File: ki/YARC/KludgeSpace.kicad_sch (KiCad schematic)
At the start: 7 parts

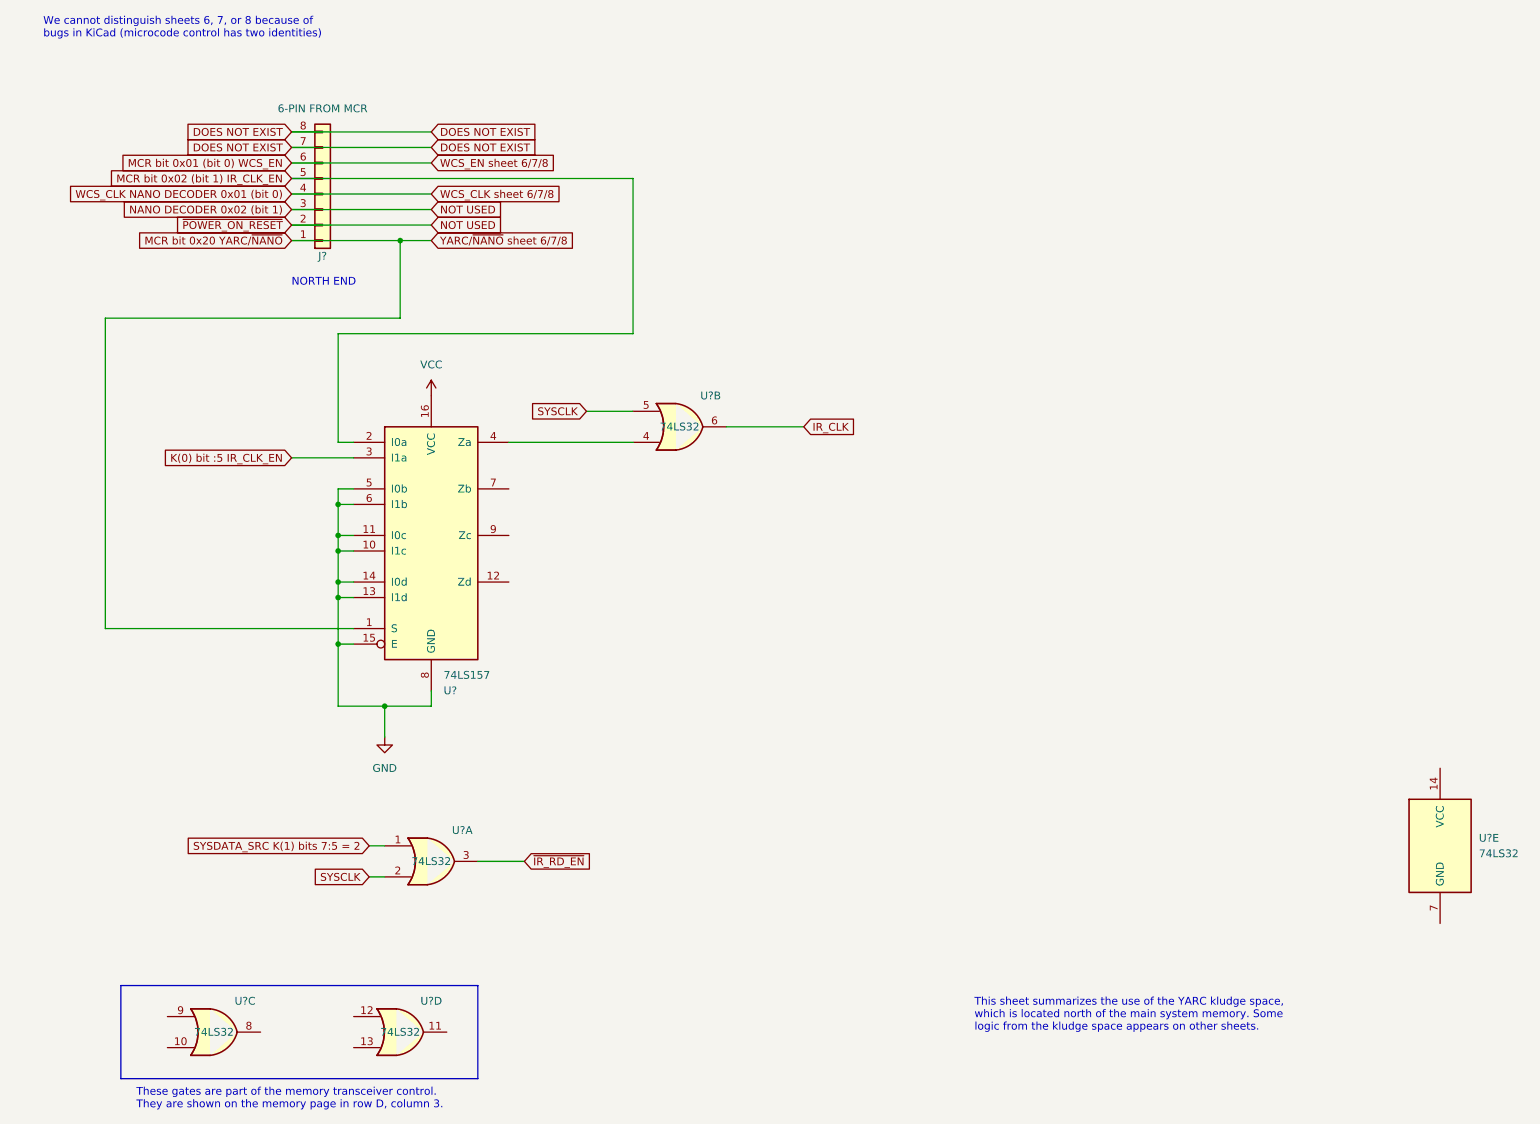
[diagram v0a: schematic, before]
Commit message: Assign part labels (U-numbers) in KiCad and start adding them to Fritzing layouts
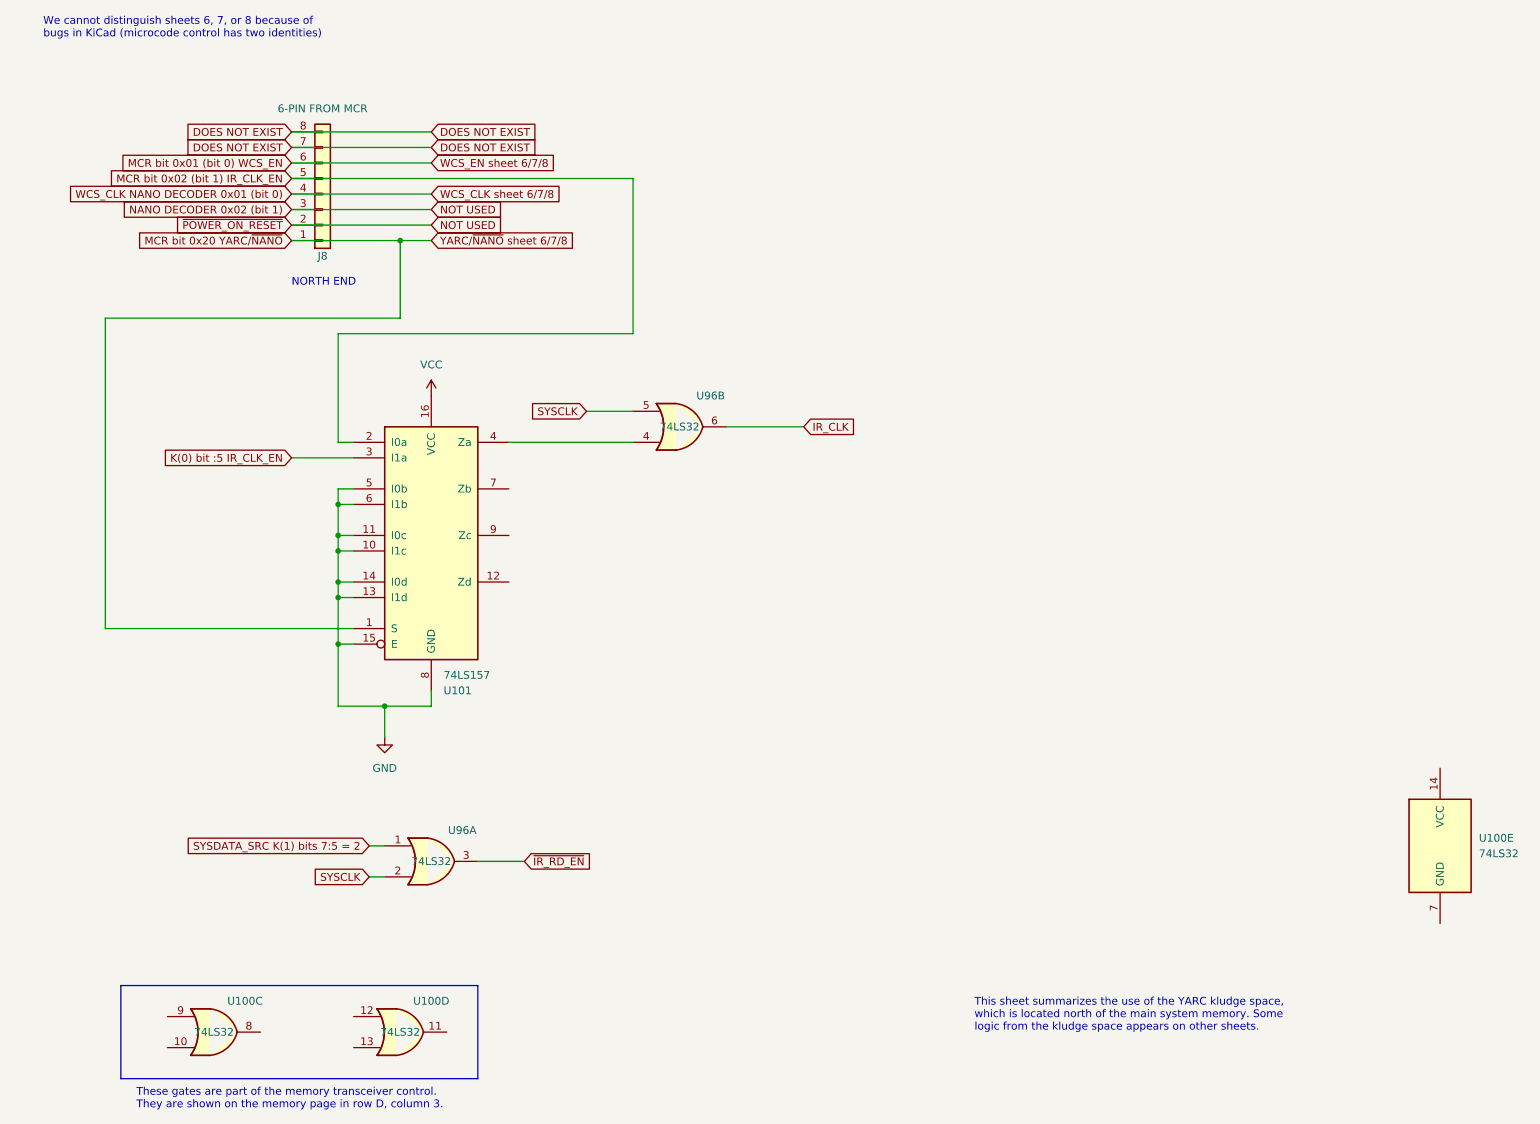
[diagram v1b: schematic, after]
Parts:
- gave numbers to parts that had none: 4
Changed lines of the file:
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@@
   (symbol (lib_id "74xx:74LS32") (at 73.66 182.88 0) (unit 4)
     (in_bom yes) (on_board yes)
-    (property "Reference" "U?" (id 0) (at 78.74 177.8 0))
+    (property "Reference" "U100" (id 0) (at 78.74 177.8 0))
     (property "Value" "74LS32" (id 1) (at 73.66 182.88 0))
     (property "Footprint" "" (id 2) (at 73.66 182.88 0)
@@
   (symbol (lib_id "power:VCC") (at 78.74 78.74 0) (unit 1)
     (in_bom yes) (on_board yes) (fields_autoplaced)
-    (property "Reference" "#PWR?" (id 0) (at 78.74 82.55 0)
+    (property "Reference" "#PWR0172" (id 0) (at 78.74 82.55 0)
       (effects (font (size 1.27 1.27)) hide)
     )
@@
   (symbol (lib_id "74xx:74LS32") (at 43.18 182.88 0) (unit 3)
     (in_bom yes) (on_board yes)
-    (property "Reference" "U?" (id 0) (at 48.26 177.8 0))
+    (property "Reference" "U100" (id 0) (at 48.26 177.8 0))
     (property "Value" "74LS32" (id 1) (at 43.18 182.88 0))
     (property "Footprint" "" (id 2) (at 43.18 182.88 0)
@@
   (symbol (lib_id "74xx:74LS32") (at 78.74 154.94 0) (unit 1)
     (in_bom yes) (on_board yes)
-    (property "Reference" "U?" (id 0) (at 83.82 149.86 0))
+    (property "Reference" "U96" (id 0) (at 83.82 149.86 0))
     (property "Value" "74LS32" (id 1) (at 78.74 154.94 0))
     (property "Footprint" "" (id 2) (at 78.74 154.94 0)
@@
   (symbol (lib_id "74xx:74LS32") (at 243.84 152.4 0) (unit 5)
     (in_bom yes) (on_board yes) (fields_autoplaced)
-    (property "Reference" "U?" (id 0) (at 250.19 151.1299 0)
+    (property "Reference" "U100" (id 0) (at 250.19 151.1299 0)
       (effects (font (size 1.27 1.27)) (justify left))
     )
@@
   (symbol (lib_id "74xx:74LS157") (at 78.74 101.6 0) (unit 1)
     (in_bom yes) (on_board yes) (fields_autoplaced)
-    (property "Reference" "U?" (id 0) (at 80.7594 127 0)
+    (property "Reference" "U101" (id 0) (at 80.7594 127 0)
       (effects (font (size 1.27 1.27)) (justify left))
     )
@@
   (symbol (lib_id "74xx:74LS32") (at 119.38 83.82 0) (mirror x) (unit 2)
     (in_bom yes) (on_board yes)
-    (property "Reference" "U?" (id 0) (at 124.46 78.74 0))
+    (property "Reference" "U96" (id 0) (at 124.46 78.74 0))
     (property "Value" "74LS32" (id 1) (at 119.38 83.82 0))
     (property "Footprint" "" (id 2) (at 119.38 83.82 0)
@@
   (symbol (lib_id "power:GND") (at 71.12 134.62 0) (unit 1)
     (in_bom yes) (on_board yes) (fields_autoplaced)
-    (property "Reference" "#PWR?" (id 0) (at 71.12 140.97 0)
+    (property "Reference" "#PWR0171" (id 0) (at 71.12 140.97 0)
       (effects (font (size 1.27 1.27)) hide)
     )
@@
   (symbol (lib_id "Connector_Generic:Conn_01x08") (at 60.96 45.72 0) (mirror x) (unit 1)
     (in_bom yes) (on_board yes)
-    (property "Reference" "J?" (id 0) (at 60.96 55.88 0))
+    (property "Reference" "J8" (id 0) (at 60.96 55.88 0))
     (property "Value" "6-PIN FROM MCR" (id 1) (at 60.96 31.75 0))
     (property "Footprint" "" (id 2) (at 60.96 45.72 0)

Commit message: Minor changes while wiring Port1 address transceiver
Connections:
- net GND: no longer U101.14 (I0d)
- net VCC: now also U101.14 (I0d)
- net ~{ADDRESS_XCVR_EN}: now reaches U101.12 (Zd)
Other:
- note added: "The effect of the "D" unit is merely to invert YARC/NANO# But it allows for future expansion (in case something else ever needs to drive the address bus when YARC)."
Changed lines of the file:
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@@
   (junction (at 63.5 119.38) (diameter 0) (color 0 0 0 0)
   )
+  (junction (at 78.74 78.74) (diameter 0) (color 0 0 0 0)
+  )
   (junction (at 63.5 101.6) (diameter 0) (color 0 0 0 0)
   )
@@
   (junction (at 63.5 104.14) (diameter 0) (color 0 0 0 0)
   )
+  (junction (at 63.5 111.76) (diameter 0) (color 0 0 0 0)
+  )
   (junction (at 73.66 53.34) (diameter 0) (color 0 0 0 0)
   )
-  (junction (at 63.5 111.76) (diameter 0) (color 0 0 0 0)
-  )
   (junction (at 71.12 129.54) (diameter 0) (color 0 0 0 0)
   )
-  (junction (at 63.5 109.22) (diameter 0) (color 0 0 0 0)
-  )
   (wire (pts (xy 104.14 81.28) (xy 111.76 81.28))
     (stroke (width 0) (type default) (color 0 0 0 0))
@@
     (stroke (width 0) (type default) (color 0 0 0 0))
   )
-  (wire (pts (xy 63.5 109.22) (xy 63.5 111.76))
-    (stroke (width 0) (type default) (color 0 0 0 0))
-  )
   (wire (pts (xy 66.04 101.6) (xy 63.5 101.6))
     (stroke (width 0) (type default) (color 0 0 0 0))
@@
     (stroke (width 0) (type default) (color 0 0 0 0))
   )
-  (wire (pts (xy 66.04 86.36) (xy 63.5 86.36))
+  (wire (pts (xy 58.42 86.36) (xy 66.04 86.36))
     (stroke (width 0) (type default) (color 0 0 0 0))
   )
@@
     (stroke (width 0) (type default) (color 0 0 0 0))
   )
-  (wire (pts (xy 63.5 119.38) (xy 63.5 111.76))
-    (stroke (width 0) (type default) (color 0 0 0 0))
-  )
   (wire (pts (xy 111.76 68.58) (xy 111.76 43.18))
     (stroke (width 0) (type default) (color 0 0 0 0))
   )
+  (wire (pts (xy 91.44 109.22) (xy 129.54 109.22))
+    (stroke (width 0) (type default) (color 0 0 0 0))
+  )
   (wire (pts (xy 73.66 53.34) (xy 78.74 53.34))
     (stroke (width 0) (type default) (color 0 0 0 0))
@@
     (stroke (width 0) (type default) (color 0 0 0 0))
   )
-  (wire (pts (xy 63.5 86.36) (xy 63.5 68.58))
-    (stroke (width 0) (type default) (color 0 0 0 0))
-  )
   (wire (pts (xy 55.88 53.34) (xy 73.66 53.34))
     (stroke (width 0) (type default) (color 0 0 0 0))
   )
+  (wire (pts (xy 60.96 109.22) (xy 60.96 78.74))
+    (stroke (width 0) (type default) (color 0 0 0 0))
+  )
   (wire (pts (xy 63.5 96.52) (xy 63.5 101.6))
     (stroke (width 0) (type default) (color 0 0 0 0))
@@
     (stroke (width 0) (type default) (color 0 0 0 0))
   )
+  (wire (pts (xy 91.44 86.36) (xy 111.76 86.36))
+    (stroke (width 0) (type default) (color 0 0 0 0))
+  )
+  (wire (pts (xy 58.42 68.58) (xy 58.42 86.36))
+    (stroke (width 0) (type default) (color 0 0 0 0))
+  )
+  (wire (pts (xy 78.74 48.26) (xy 55.88 48.26))
+    (stroke (width 0) (type default) (color 0 0 0 0))
+  )
   (wire (pts (xy 66.04 111.76) (xy 63.5 111.76))
     (stroke (width 0) (type default) (color 0 0 0 0))
   )
-  (wire (pts (xy 91.44 86.36) (xy 111.76 86.36))
-    (stroke (width 0) (type default) (color 0 0 0 0))
-  )
-  (wire (pts (xy 78.74 48.26) (xy 55.88 48.26))
-    (stroke (width 0) (type default) (color 0 0 0 0))
-  )
   (wire (pts (xy 78.74 50.8) (xy 55.88 50.8))
     (stroke (width 0) (type default) (color 0 0 0 0))
@@
     (stroke (width 0) (type default) (color 0 0 0 0))
   )
-  (wire (pts (xy 66.04 88.9) (xy 55.88 88.9))
+  (wire (pts (xy 66.04 88.9) (xy 53.34 88.9))
     (stroke (width 0) (type default) (color 0 0 0 0))
   )
@@
     (stroke (width 0) (type default) (color 0 0 0 0))
   )
+  (wire (pts (xy 63.5 111.76) (xy 63.5 119.38))
+    (stroke (width 0) (type default) (color 0 0 0 0))
+  )
   (wire (pts (xy 127 83.82) (xy 139.7 83.82))
     (stroke (width 0) (type default) (color 0 0 0 0))
@@
     (stroke (width 0) (type default) (color 0 0 0 0))
   )
-  (wire (pts (xy 66.04 109.22) (xy 63.5 109.22))
-    (stroke (width 0) (type default) (color 0 0 0 0))
-  )
   (wire (pts (xy 78.74 45.72) (xy 55.88 45.72))
     (stroke (width 0) (type default) (color 0 0 0 0))
@@
     (stroke (width 0) (type default) (color 0 0 0 0))
   )
+  (wire (pts (xy 66.04 109.22) (xy 60.96 109.22))
+    (stroke (width 0) (type default) (color 0 0 0 0))
+  )
+  (wire (pts (xy 60.96 78.74) (xy 78.74 78.74))
+    (stroke (width 0) (type default) (color 0 0 0 0))
+  )
   (wire (pts (xy 71.12 129.54) (xy 78.74 129.54))
     (stroke (width 0) (type default) (color 0 0 0 0))
   )
-  (wire (pts (xy 63.5 104.14) (xy 63.5 109.22))
+  (wire (pts (xy 63.5 104.14) (xy 63.5 111.76))
     (stroke (width 0) (type default) (color 0 0 0 0))
   )
@@
     (stroke (width 0) (type default) (color 0 0 0 0))
   )
-  (wire (pts (xy 63.5 68.58) (xy 111.76 68.58))
+  (wire (pts (xy 58.42 68.58) (xy 111.76 68.58))
     (stroke (width 0) (type default) (color 0 0 0 0))
   )
@@
   )
   (text "NORTH END" (at 55.88 60.96 0)
+    (effects (font (size 1.27 1.27)) (justify left bottom))
+  )
+  (text "The effect of the \"D\" unit is merely to invert YARC/NANO#\nBut it allows for future expansion (in case something else\never needs to drive the address bus when YARC)."
+    (at 91.44 119.38 0)
     (effects (font (size 1.27 1.27)) (justify left bottom))
   )
@@
     )
   )
-  (global_label "K(0) bit :5 IR_CLK_EN" (shape input) (at 55.88 88.9 180) (fields_autoplaced)
+  (global_label "K(0) bit :5 IR_CLK_EN" (shape input) (at 53.34 88.9 180) (fields_autoplaced)
     (effects (font (size 1.27 1.27)) (justify right))
-    (property "Intersheet References" "${INTERSHEET_REFS}" (id 0) (at 32.2398 88.8206 0)
+    (property "Intersheet References" "${INTERSHEET_REFS}" (id 0) (at 29.6998 88.8206 0)
       (effects (font (size 1.27 1.27)) (justify right) hide)
     )
@@
     )
   )
+  (global_label "~{ADDRESS_XCVR_EN}" (shape input) (at 129.54 109.22 0) (fields_autoplaced)
+    (effects (font (size 1.27 1.27)) (justify left))
+    (property "Intersheet References" "${INTERSHEET_REFS}" (id 0) (at 149.6726 109.1406 0)
+      (effects (font (size 1.27 1.27)) (justify left) hide)
+    )
+  )

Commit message: Add register enable to MCR. Corrections and cleanups.
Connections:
- net GND: no longer U101.10 (I1c), U101.11 (I0c)
- net ~{DST_EN} to U93B: now reaches U101.9 (Zc)
- new net DS_PRE_CLK (CircuitSim): U101.10 (I1c)
- new net MCR bit 0x80 (bit 7): U101.11 (I0c)
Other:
- note added: "Temporarily, K(1) bit 0 (dst_wr_en) is directly connected to U101 pin 10. This allows the microcodeto enable register writes when YARC has control."
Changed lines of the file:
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@@
   (junction (at 78.74 78.74) (diameter 0) (color 0 0 0 0)
   )
-  (junction (at 63.5 101.6) (diameter 0) (color 0 0 0 0)
-  )
   (junction (at 63.5 96.52) (diameter 0) (color 0 0 0 0)
   )
-  (junction (at 63.5 104.14) (diameter 0) (color 0 0 0 0)
-  )
   (junction (at 63.5 111.76) (diameter 0) (color 0 0 0 0)
   )
@@
     (stroke (width 0) (type default) (color 0 0 0 0))
   )
-  (wire (pts (xy 66.04 101.6) (xy 63.5 101.6))
-    (stroke (width 0) (type default) (color 0 0 0 0))
-  )
   (polyline (pts (xy 86.36 175.26) (xy 27.94 175.26))
     (stroke (width 0) (type default) (color 0 0 0 0))
@@
     (stroke (width 0) (type default) (color 0 0 0 0))
   )
+  (wire (pts (xy 66.04 101.6) (xy 53.34 101.6))
+    (stroke (width 0) (type default) (color 0 0 0 0))
+  )
   (wire (pts (xy 73.66 66.04) (xy 73.66 53.34))
     (stroke (width 0) (type default) (color 0 0 0 0))
@@
     (stroke (width 0) (type default) (color 0 0 0 0))
   )
-  (wire (pts (xy 63.5 101.6) (xy 63.5 104.14))
-    (stroke (width 0) (type default) (color 0 0 0 0))
-  )
   (wire (pts (xy 55.88 53.34) (xy 73.66 53.34))
     (stroke (width 0) (type default) (color 0 0 0 0))
@@
     (stroke (width 0) (type default) (color 0 0 0 0))
   )
-  (wire (pts (xy 63.5 96.52) (xy 63.5 101.6))
-    (stroke (width 0) (type default) (color 0 0 0 0))
-  )
-  (wire (pts (xy 66.04 104.14) (xy 63.5 104.14))
+  (wire (pts (xy 63.5 96.52) (xy 63.5 111.76))
     (stroke (width 0) (type default) (color 0 0 0 0))
   )
@@
     (stroke (width 0) (type default) (color 0 0 0 0))
   )
+  (wire (pts (xy 66.04 104.14) (xy 53.34 104.14))
+    (stroke (width 0) (type default) (color 0 0 0 0))
+  )
   (wire (pts (xy 78.74 38.1) (xy 55.88 38.1))
     (stroke (width 0) (type default) (color 0 0 0 0))
@@
     (stroke (width 0) (type default) (color 0 0 0 0))
   )
-  (wire (pts (xy 63.5 104.14) (xy 63.5 111.76))
-    (stroke (width 0) (type default) (color 0 0 0 0))
-  )
   (wire (pts (xy 86.36 154.94) (xy 93.98 154.94))
     (stroke (width 0) (type default) (color 0 0 0 0))
@@
     (stroke (width 0) (type default) (color 0 0 0 0))
   )
+  (wire (pts (xy 91.44 101.6) (xy 127 101.6))
+    (stroke (width 0) (type default) (color 0 0 0 0))
+  )
   (wire (pts (xy 78.74 129.54) (xy 78.74 127))
     (stroke (width 0) (type default) (color 0 0 0 0))
   )
   (text "NORTH END" (at 55.88 60.96 0)
+    (effects (font (size 1.27 1.27)) (justify left bottom))
+  )
+  (text "Temporarily, K(1) bit 0 (dst_wr_en)\nis directly connected to U101 pin 10.\nThis allows the microcodeto enable\nregister writes when YARC has control."
+    (at 20.32 129.54 0)
     (effects (font (size 1.27 1.27)) (justify left bottom))
   )
@@
     )
   )
+  (global_label "MCR bit 0x80 (bit 7)" (shape input) (at 53.34 101.6 180) (fields_autoplaced)
+    (effects (font (size 1.27 1.27)) (justify right))
+    (property "Intersheet References" "${INTERSHEET_REFS}" (id 0) (at 30.5464 101.5206 0)
+      (effects (font (size 1.27 1.27)) (justify right) hide)
+    )
+  )
+  (global_label "~{DST_EN} to U93B" (shape input) (at 127 101.6 0) (fields_autoplaced)
+    (effects (font (size 1.27 1.27)) (justify left))
+    (property "Intersheet References" "${INTERSHEET_REFS}" (id 0) (at 145.1369 101.5206 0)
+      (effects (font (size 1.27 1.27)) (justify left) hide)
+    )
+  )
   (global_label "K(0) bit :5 IR_CLK_EN" (shape input) (at 53.34 88.9 180) (fields_autoplaced)
     (effects (font (size 1.27 1.27)) (justify right))
@@
       (effects (font (size 1.27 1.27)) (justify right) hide)
     )
+  )
+  (global_label "DS_PRE_CLK (CircuitSim)" (shape input) (at 53.34 104.14 180) (fields_autoplaced)
+    (effects (font (size 1.27 1.27)) (justify right))
+    (property "Intersheet References" "${INTERSHEET_REFS}" (id 0) (at 26.8574 104.0606 0)
+      (effects (font (size 1.27 1.27)) (justify right) hide)
+    )
